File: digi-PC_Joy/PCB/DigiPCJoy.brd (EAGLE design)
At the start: 37.5 x 40 mm, 7 parts

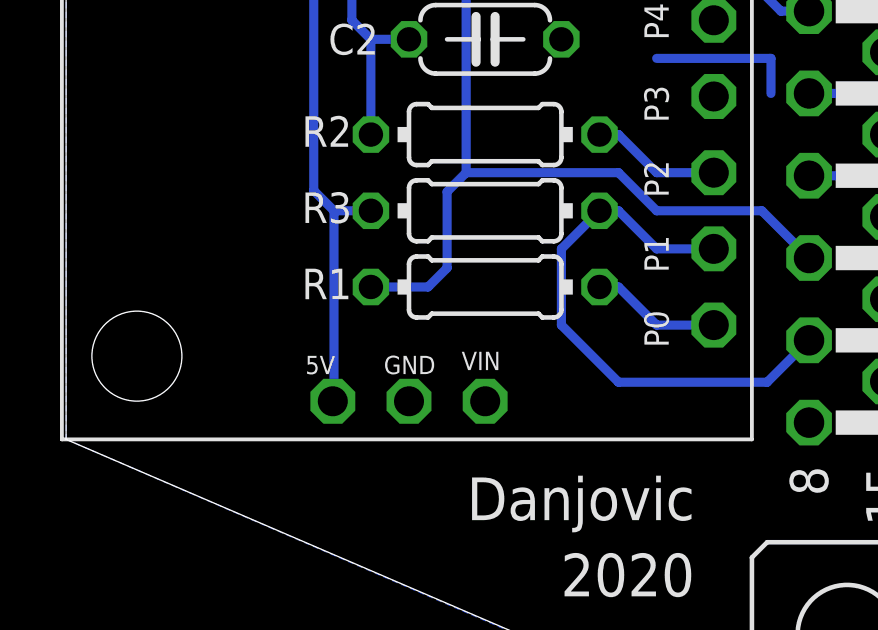
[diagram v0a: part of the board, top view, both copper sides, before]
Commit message: Updadet footprint of digispark board with USB connector
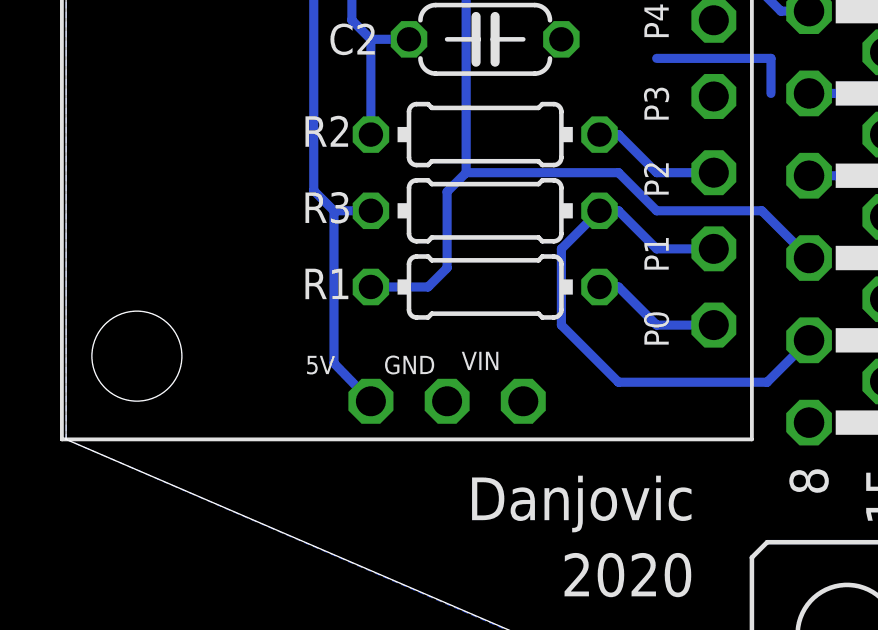
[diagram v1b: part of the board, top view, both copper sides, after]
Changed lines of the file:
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@@
 <attribute name="VALUE" x="36.195" y="28.702" size="1.778" layer="27" ratio="10" rot="R270"/>
 </element>
-<element name="B1" library="Digistump" package="DIGISPARK_SOCKET" value="Digispark" x="19.05" y="29.21" rot="R270"/>
+<element name="B1" library="Digistump" package="DIGISPARK_SOCKET" value="Digispark" x="19.05" y="29.21" smashed="yes" rot="R270">
+<attribute name="NAME" x="20.32" y="29.21" size="1.27" layer="25" rot="R270"/>
+</element>
 </elements>
 <signals>
@@
 <wire x1="4.445" y1="18.453440625" x2="5.118440625" y2="17.78" width="0.3048" layer="16"/>
 <contactref element="B1" pad="5V"/>
-<wire x1="5.08" y1="11.43" x2="5.118440625" y2="11.43" width="0.3048" layer="16"/>
-<wire x1="5.118440625" y1="11.43" x2="5.118440625" y2="17.78" width="0.3048" layer="16"/>
+<wire x1="6.35" y1="11.43" x2="5.118440625" y2="12.7" width="0.3048" layer="16"/>
+<wire x1="5.118440625" y1="12.7" x2="5.118440625" y2="17.78" width="0.3048" layer="16"/>
 </signal>
 <signal name="GND">

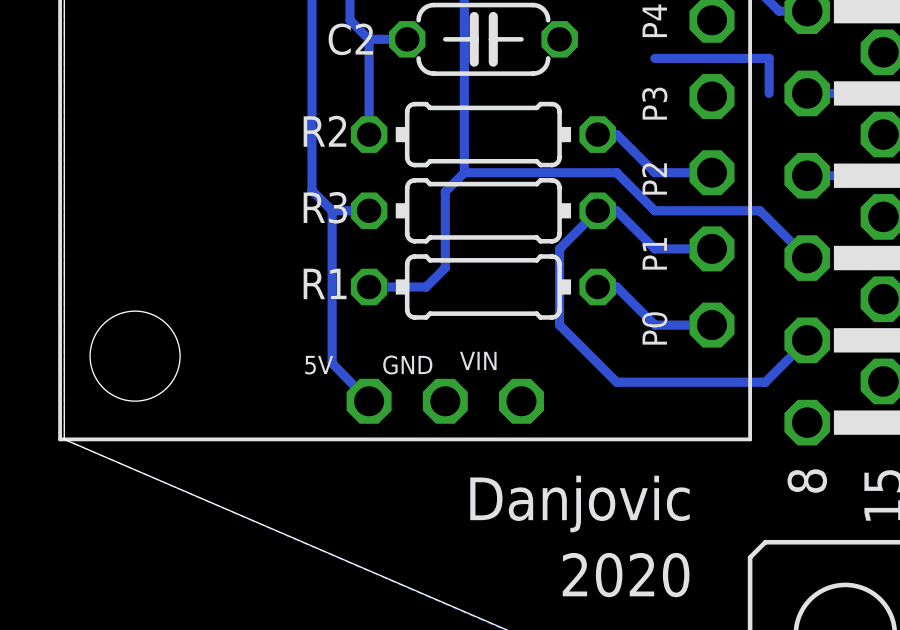
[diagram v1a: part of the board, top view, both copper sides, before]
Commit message: updated digispark footprint
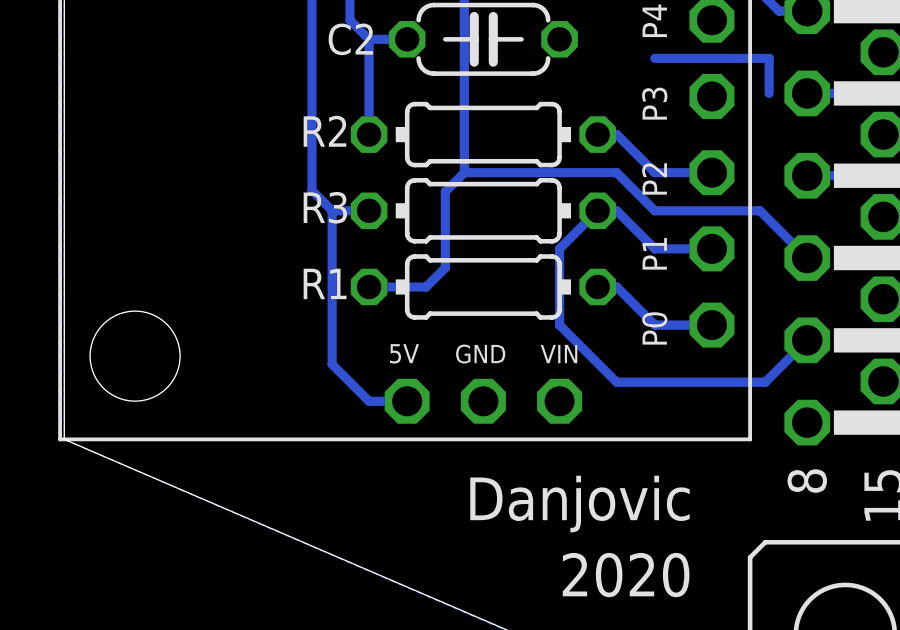
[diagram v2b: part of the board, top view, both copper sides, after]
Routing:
- net +5V: track 36.2 -> 37.5 mm
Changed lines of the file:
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@@
 <text x="16.278440625" y="23.470578125" size="0.8128" layer="21" rot="R90">P4</text>
 <text x="16.278440625" y="25.970578125" size="0.8128" layer="21" rot="R90">P5</text>
-<text x="4.163440625" y="12.335578125" size="0.6096" layer="21">5V</text>
-<text x="9.373440625" y="12.470578125" size="0.6096" layer="21">VIN</text>
-<text x="6.778440625" y="12.335578125" size="0.6096" layer="21">GND</text>
+<text x="6.985" y="12.7" size="0.635" layer="21">5V</text>
+<text x="12.065" y="12.7" size="0.6096" layer="21">VIN</text>
+<text x="9.2075" y="12.7" size="0.6096" layer="21">GND</text>
 <text x="17.145" y="32.385" size="1.4224" layer="21" font="vector" ratio="15" rot="R180">DigiPCJoy</text>
 <text x="17.145" y="8.89" size="1.4224" layer="21" font="vector" ratio="15" rot="R180">Danjovic</text>
@@
 <wire x1="4.445" y1="18.453440625" x2="5.118440625" y2="17.78" width="0.3048" layer="16"/>
 <contactref element="B1" pad="5V"/>
-<wire x1="6.35" y1="11.43" x2="5.118440625" y2="12.7" width="0.3048" layer="16"/>
-<wire x1="5.118440625" y1="12.7" x2="5.118440625" y2="17.78" width="0.3048" layer="16"/>
+<wire x1="7.62" y1="11.43" x2="6.35" y2="11.43" width="0.3048" layer="16"/>
+<wire x1="6.35" y1="11.43" x2="5.118440625" y2="12.661559375" width="0.3048" layer="16"/>
+<wire x1="5.118440625" y1="12.661559375" x2="5.118440625" y2="17.78" width="0.3048" layer="16"/>
 </signal>
 <signal name="GND">
